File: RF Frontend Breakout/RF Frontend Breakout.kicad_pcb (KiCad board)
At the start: 2 copper layers, 122.5 x 83 mm, 54 parts, among them IC1 QPC1022SR, IC2 GRF5504, IC3 LHA-13LN+, IC4 QPC1022SR, J3 Conn_Coaxial, J4 Conn_01x02, J5 Conn_01x02, J6 Conn_Coaxial

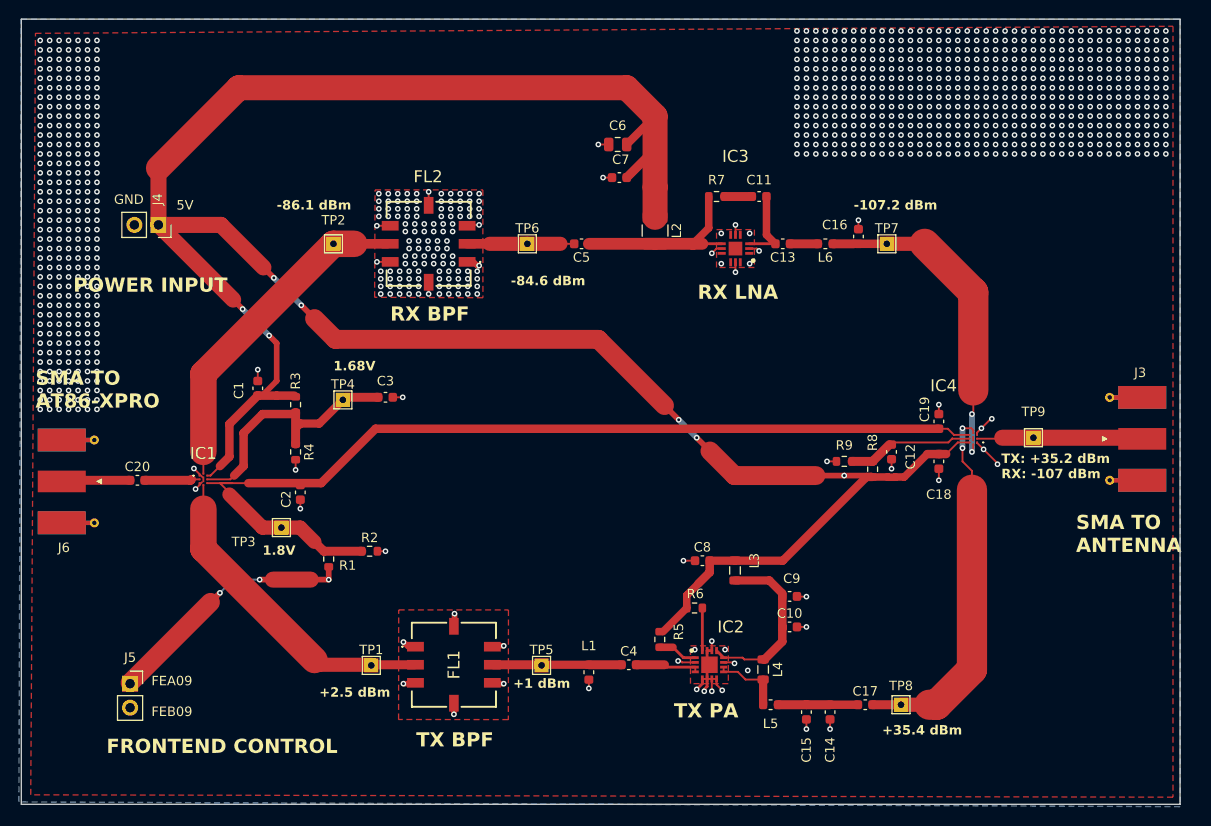
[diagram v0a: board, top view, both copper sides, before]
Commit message: finished frontend layout!
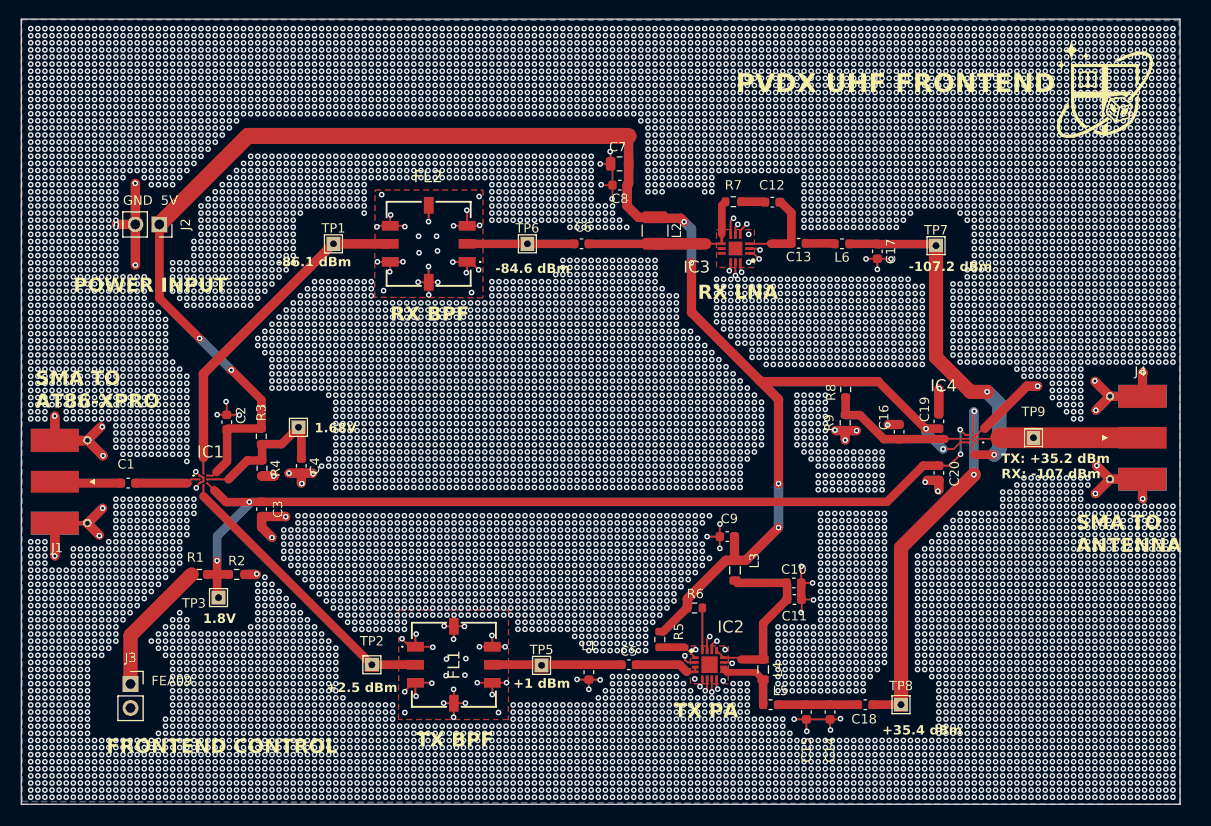
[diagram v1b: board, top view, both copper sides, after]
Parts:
- removed J5: Conn_01x02, Connector_PinSocket_2.54mm:PinSocket_1x02_P2.54mm_Vertical
- removed J6: Conn_Coaxial, Connector_Coaxial:SMA_Molex_73251-1153_EdgeMount_Horizontal
- added G***: LOGO, Logo:bse_logo, F.Cu at (190.6, 79.5)
- added J1: Conn_Coaxial, Connector_Coaxial:SMA_Molex_73251-1153_EdgeMount_Horizontal, F.Cu at (81.3, 120.7)
- added J2: Conn_01x02, Connector_PinSocket_2.54mm:PinSocket_1x02_P2.54mm_Vertical, F.Cu at (90.6, 93.5)
- C1: value 100n -> 0.8p
- C10, C12: value 100p -> 0.1u
- C11: value 0.1u -> 100p
- C16: value 1.5p -> 100p
- C17: value 100p -> 1.5p
- C18: value 2.2n -> 100p
- C19: value 100p -> 2.2n
- C2: value 100p -> 100n
- C20: value 0.8p -> 100p
- C4: value 20p -> 100p
- C5: value 2.2u -> 20p
- C6: value 10u -> 2.2u; footprint Capacitor_SMD:C_0805_2012Metric -> Capacitor_SMD:C_0603_1608Metric
- C7: value 1n -> 10u; footprint Capacitor_SMD:C_0603_1608Metric -> Capacitor_SMD:C_0805_2012Metric
- C8: value 0.1u -> 1n
- J3: value Conn_Coaxial -> Conn_01x02; footprint Connector_Coaxial:SMA_Molex_73251-1153_EdgeMount_Horizontal -> Connector_PinSocket_2.54mm:PinSocket_1x02_P2.54mm_Vertical
- J4: value Conn_01x02 -> Conn_Coaxial; footprint Connector_PinSocket_2.54mm:PinSocket_1x02_P2.54mm_Vertical -> Connector_Coaxial:SMA_Molex_73251-1153_EdgeMount_Horizontal
- moved J3 108.4 mm to (87.5, 142.0), turned to 0 degrees
- moved J4 104.8 mm to (192.8, 116.0), turned to 180 degrees
- moved C20 84.7 mm to (173.0, 119.7), turned to -90 degrees
- moved C17 47.9 mm to (166.5, 96.3), turned to -90 degrees
- moved C5 44.8 mm to (140.2, 140.0), turned to 0 degrees
- moved TP1 44.7 mm to (109.0, 95.5)
- moved TP2 44.7 mm to (113.1, 140.0)
- moved C11 42.8 mm to (157.7, 133.1), turned to 0 degrees
- moved C8 40.6 mm to (139.3, 89.3), turned to 180 degrees
- moved C4 40.5 mm to (105.6, 119.0), turned to -90 degrees
- moved C12 29.3 mm to (155.4, 91.1), turned to 180 degrees
- moved C18 26.9 mm to (165.2, 144.2), turned to 0 degrees
- moved C16 21.1 mm to (168.8, 115.4)
- moved C3 17.6 mm to (101.4, 123.5), turned to -90 degrees
- moved C1 17.0 mm to (87.3, 120.8), turned to 0 degrees
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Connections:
- C1 pad 1: +5V -> Net-(J1-In)
- C1 pad 2: GND -> Net-(IC1-ANT)
- C11 pad 1: Net-(IC3-RF-IN) -> Net-(IC2-BIAS)
- C11 pad 2: Net-(C11-Pad2) -> GND
- C12 pad 1: Net-(IC4-EN) -> Net-(IC3-RF-IN)
- C12 pad 2: GND -> Net-(C12-Pad2)
- C16 pad 1: Net-(IC4-RF2) -> Net-(IC4-EN)
- C17 pad 1: Net-(C14-Pad1) -> Net-(IC4-RF2)
- C17 pad 2: Net-(IC4-RF1) -> GND
- C18 pad 1: +5V -> Net-(C14-Pad1)
- C18 pad 2: GND -> Net-(IC4-RF1)
- C19 pad 1: Net-(IC1-CTRL) -> +5V
- C2 pad 1: Net-(IC1-CTRL) -> +5V
- C20 pad 1: Net-(J6-In) -> Net-(IC1-CTRL)
- C20 pad 2: Net-(IC1-ANT) -> GND
- C3 pad 1: Net-(IC1-EN) -> Net-(IC1-CTRL)
- C4 pad 1: Net-(FL1-RF_OUT) -> Net-(IC1-EN)
- C4 pad 2: Net-(IC2-RF_IN_1) -> GND
- C5 pad 1: Net-(IC3-RF-OUT&DC-IN) -> Net-(FL1-RF_OUT)
- C5 pad 2: Net-(FL2-RF_IN) -> Net-(IC2-RF_IN_1)
- C6 pad 1: +5V -> Net-(IC3-RF-OUT&DC-IN)
- C6 pad 2: GND -> Net-(FL2-RF_IN)
- C8 pad 1: GND -> +5V
- C8 pad 2: +5V -> GND
- C9 pad 1: Net-(IC2-BIAS) -> GND
- C9 pad 2: GND -> +5V
- J3 pad 1: Net-(IC4-ANT) -> /FEA09
- J3 pad 2: GND -> /FEB09
- J4 pad 1: +5V -> Net-(IC4-ANT)
- R7 pad 1: Net-(C11-Pad2) -> Net-(C12-Pad2)
- TP1 pad 1: Net-(FL1-RF_IN) -> Net-(FL2-RF_OUT)
- TP2 pad 1: Net-(FL2-RF_OUT) -> Net-(FL1-RF_IN)
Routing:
- net GND: track 61.6 -> 196.1 mm, vias 1008 -> 12730
- net +5V: track 251.2 -> 186.4 mm, vias 7 -> 8
- net /FEA09: track 27.0 -> 14.3 mm, vias 3 -> 0
- net Net-(IC1-EN): track 27.8 -> 15.9 mm
- net Net-(J6-In): track 7.27 -> 0.00 mm
- net Net-(J1-In): track 0.00 -> 6.86 mm
- net Net-(IC4-RF2): track 34.8 -> 38.3 mm
- net Net-(IC4-ANT): track 21.5 -> 18.1 mm
- net Net-(FL1-RF_IN): track 34.3 -> 31.0 mm
- net Net-(C11-Pad2): track 2.90 -> 0.00 mm
- net Net-(IC4-EN): track 13.4 -> 16.0 mm
- net Net-(C12-Pad2): track 0.00 -> 2.47 mm
- net Net-(FL2-RF_OUT): track 37.9 -> 36.0 mm
- net Net-(IC3-RF-IN): track 8.19 -> 9.34 mm
- net Net-(IC3-RF-OUT&DC-IN): track 19.7 -> 18.7 mm
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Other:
- board text added: "IC1"
- board text added: "PVDX UHF FRONTEND"
- board text removed: "+5V"
- board text removed: "FEB09"
